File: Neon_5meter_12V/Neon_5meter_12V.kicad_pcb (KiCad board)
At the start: 2 copper layers, 46 parts, among them J1 Conn_01x16_Pin, J2 Barrel_Jack_MountingPin, J3 Conn_01x16_Pin, J4 Barrel_Jack_MountingPin, J5 Barrel_Jack_MountingPin, J6 Conn_01x03_Pin, Q1 IRLML2502TRPBF, Q2 IRLML2502TRPBF, Q3 BSS138, Q4 BSS138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

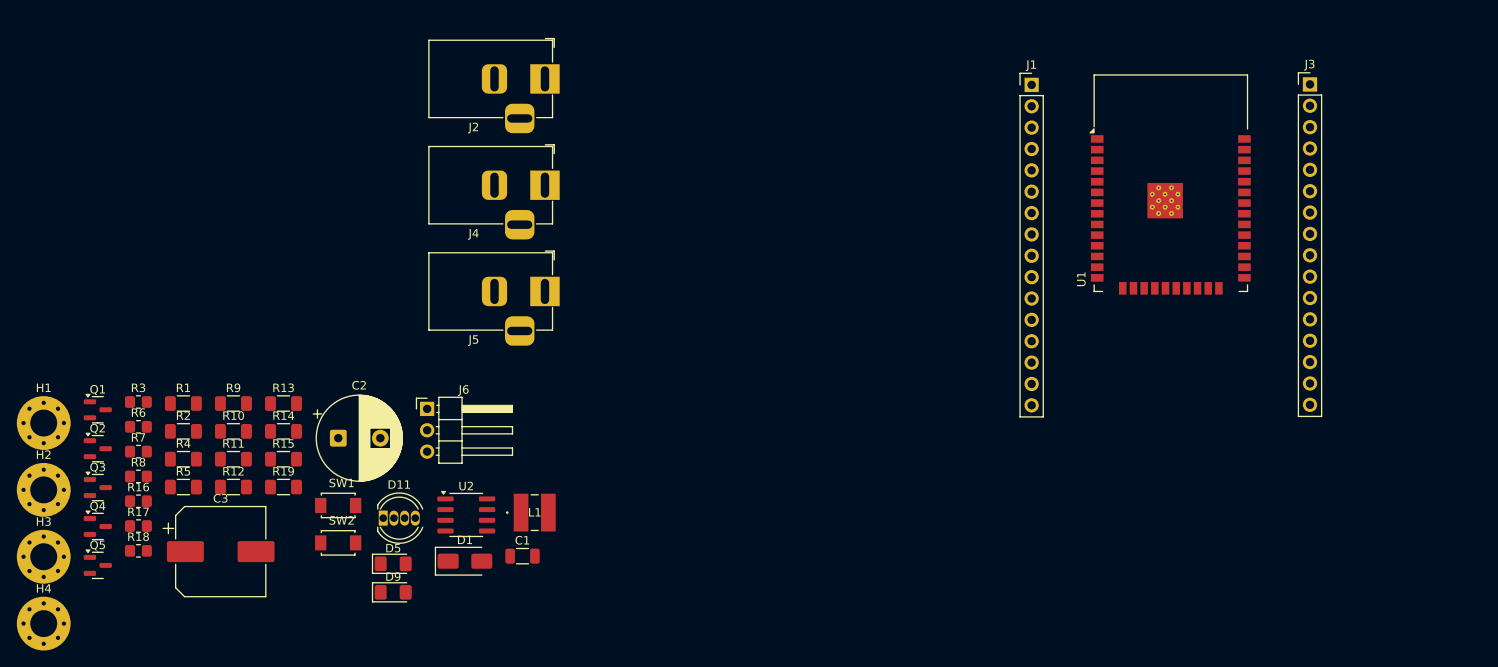
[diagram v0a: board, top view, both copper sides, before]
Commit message: updated component placement
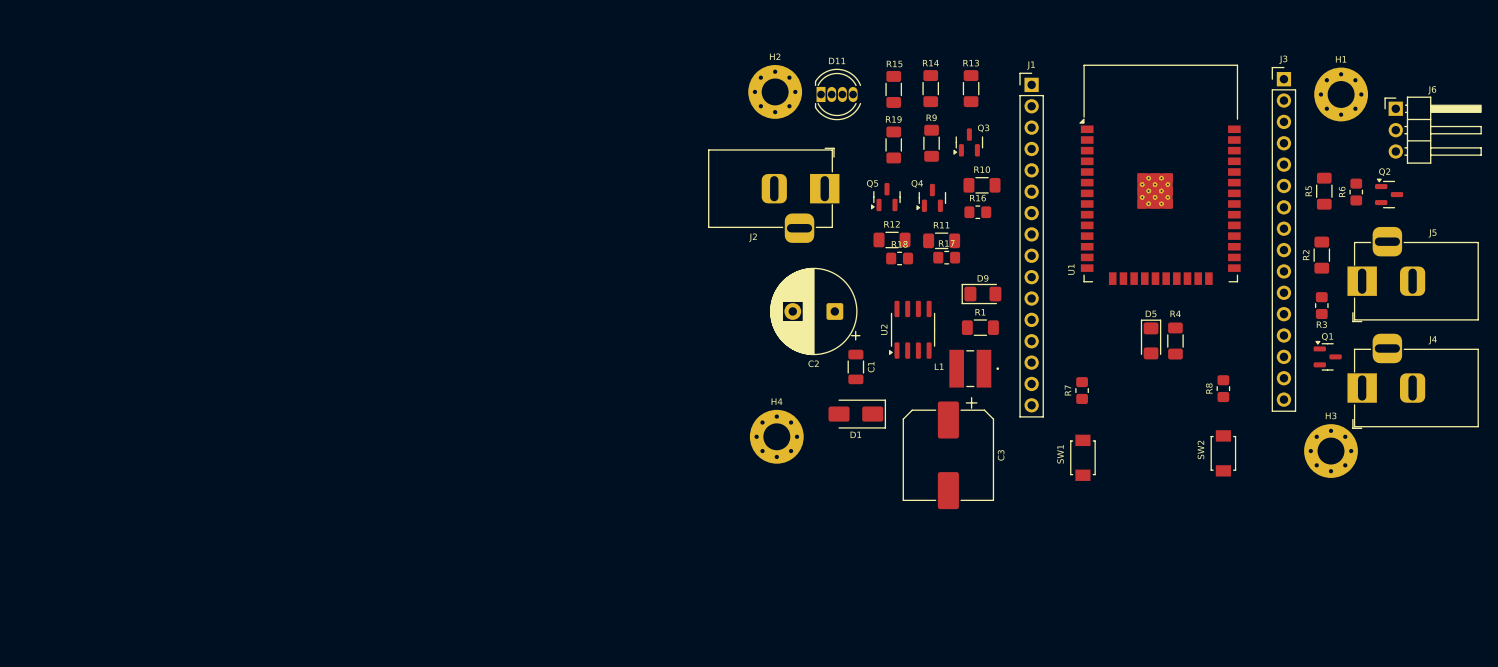
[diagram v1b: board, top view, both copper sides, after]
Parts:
- moved H1 159.1 mm to (183.6, 38.1)
- moved Q2 156.5 mm to (189.3, 50.0)
- moved H3 153.6 mm to (182.4, 80.5)
- moved R6 147.5 mm to (185.4, 49.7), turned to 90 degrees
- moved Q1 146.4 mm to (182.0, 69.3)
- moved R3 141.2 mm to (181.3, 63.2), turned to -90 degrees
- moved R5 140.1 mm to (181.6, 49.6), turned to 90 degrees
- moved R2 137.0 mm to (181.3, 57.2), turned to 90 degrees
- moved R8 129.4 mm to (169.6, 73.1), turned to 90 degrees
- moved J6 120.6 mm to (190.1, 39.8)
- moved R4 118.8 mm to (163.9, 67.4), turned to 90 degrees
- moved R7 112.4 mm to (152.8, 73.3), turned to 90 degrees
- moved Q3 111.5 mm to (139.4, 43.8), turned to 90 degrees
- moved Q4 106.6 mm to (135.0, 50.4), turned to 90 degrees
- moved SW2 105.8 mm to (169.6, 80.8), turned to 90 degrees
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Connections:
- R5 pad 2: ESP_IO18 -> ESP_IO19

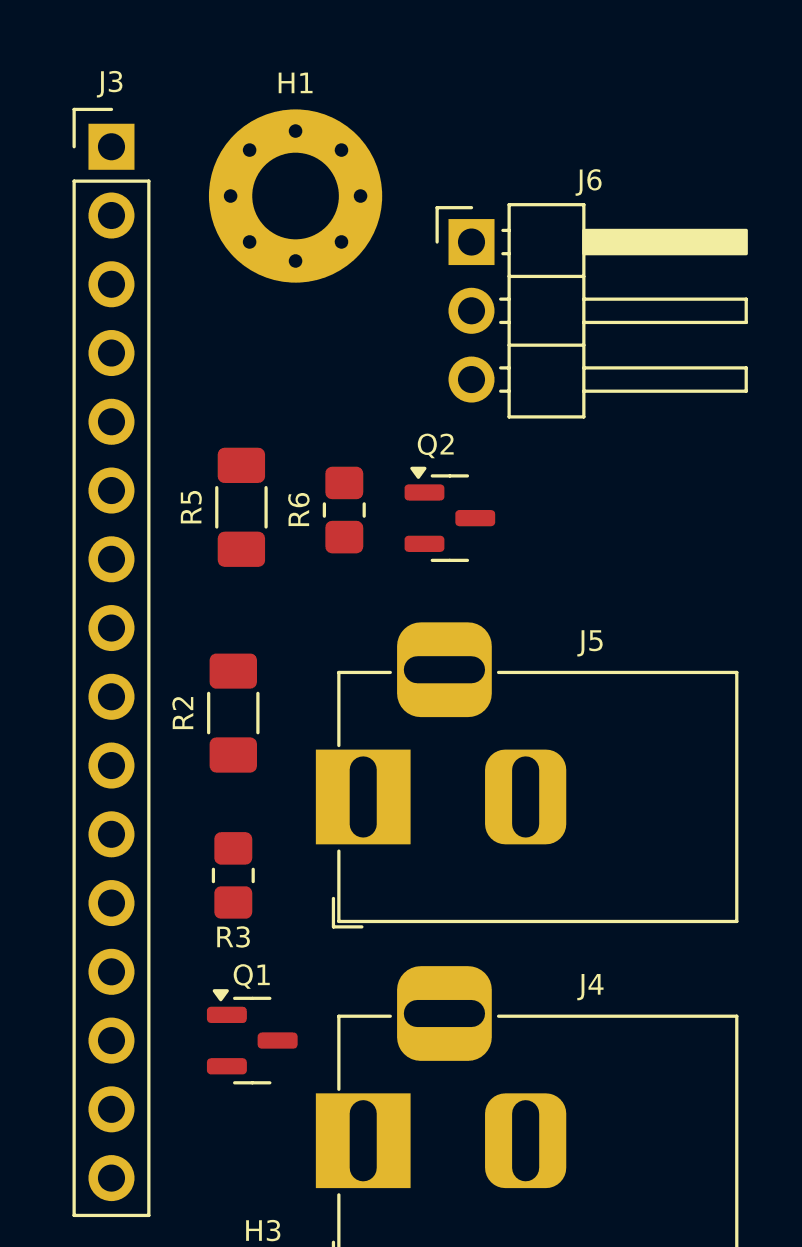
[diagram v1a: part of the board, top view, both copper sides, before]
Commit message: updated 1x3 pin header jst connector footprint
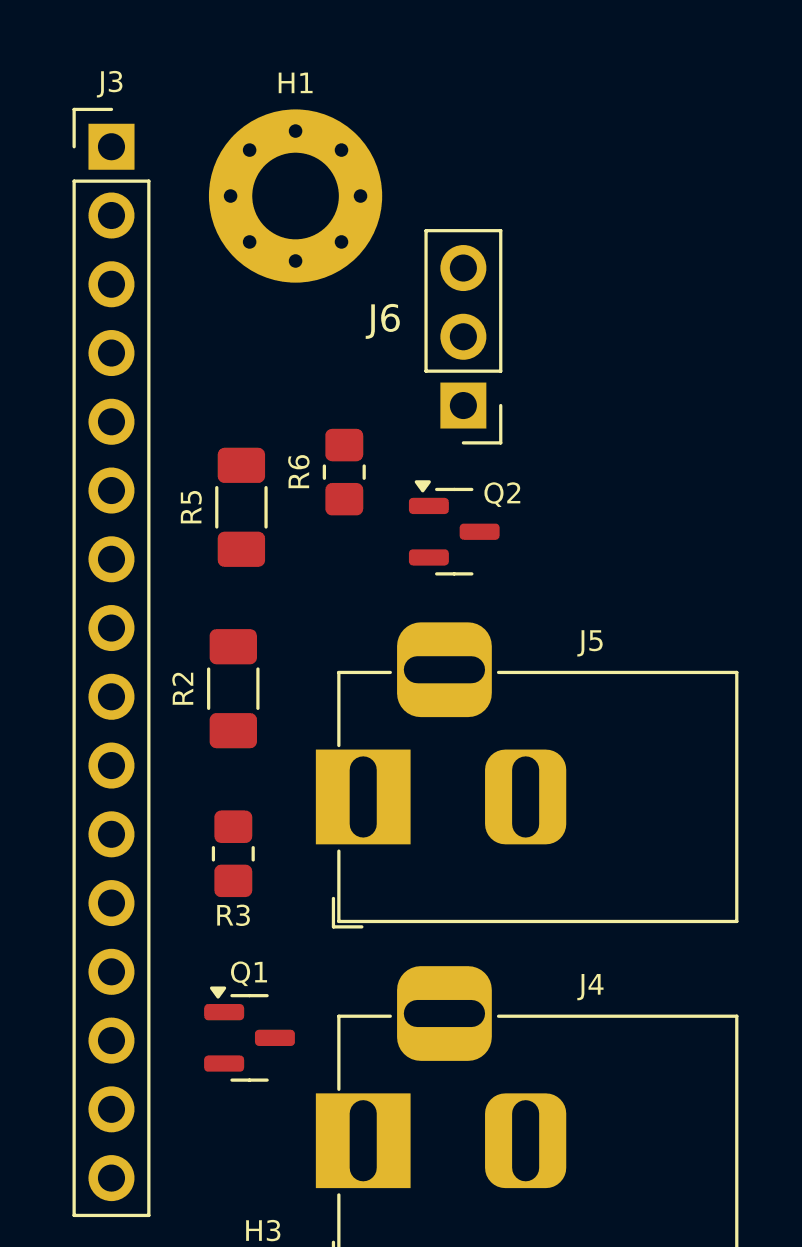
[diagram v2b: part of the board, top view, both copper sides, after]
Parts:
- J6: footprint Connector_PinHeader_2.54mm:PinHeader_1x03_P2.54mm_Horizontal -> Connector_PinHeader_2.54mm:PinHeader_1x03_P2.54mm_Vertical
- moved J6 6.05 mm to (189.8, 45.8), turned to 180 degrees
- moved R6 1.40 mm to (185.4, 48.3)
- moved R2 0.90 mm to (181.3, 56.3)
- moved R3 0.80 mm to (181.3, 62.4)
- moved Q2 0.53 mm to (189.5, 50.5)
- moved Q1 0.14 mm to (181.9, 69.2)

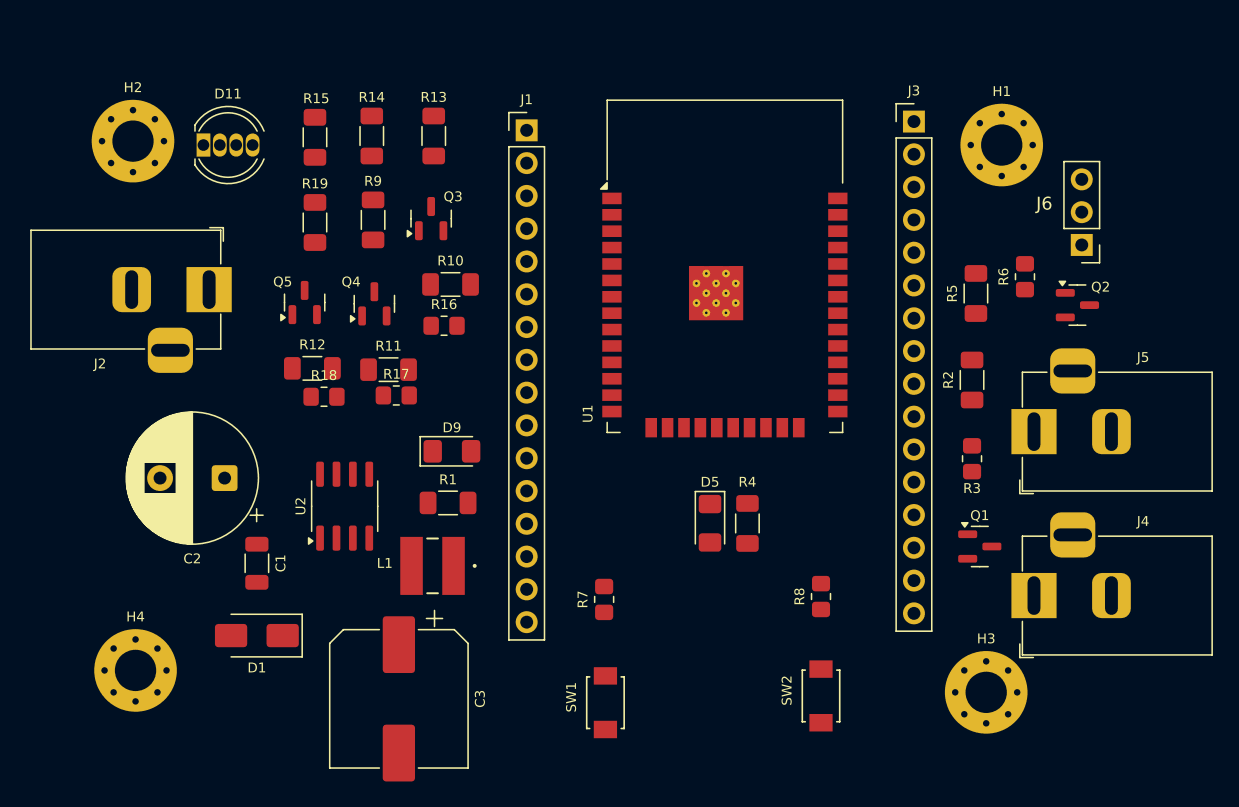
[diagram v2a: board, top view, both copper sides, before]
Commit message: updated placement removed pinheaders
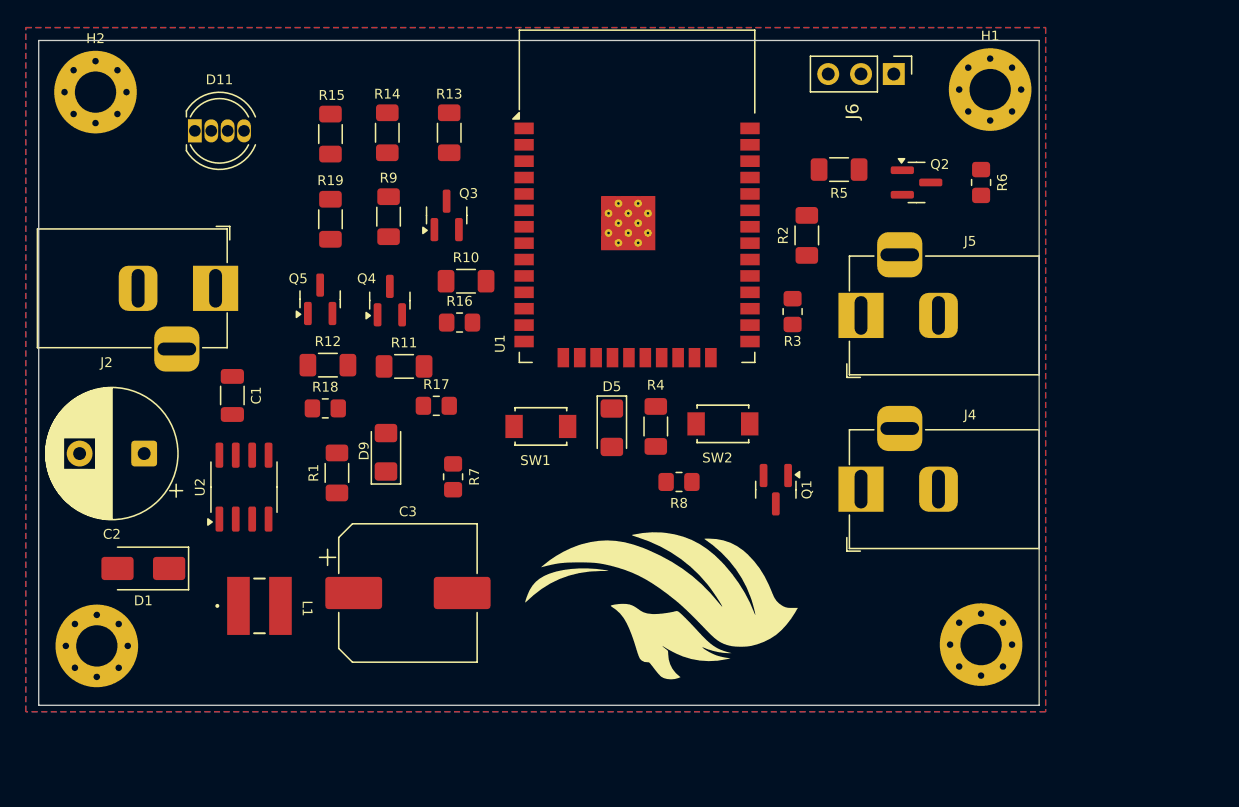
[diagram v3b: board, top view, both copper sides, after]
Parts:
- removed J1, J3: Conn_01x16_Pin, Connector_PinHeader_2.54mm:PinHeader_1x16_P2.54mm_Vertical
- added G***: LOGO, LOGO, F.Cu at (157.2, 72.9)
- moved SW2 22.4 mm to (162.0, 59.7), turned to 180 degrees
- moved SW1 22.0 mm to (147.9, 59.9), turned to 180 degrees
- moved J6 19.7 mm to (175.2, 32.6), turned to -90 degrees
- moved R3 18.0 mm to (167.4, 51.0)
- moved R2 17.0 mm to (168.5, 45.1)
- moved Q1 16.4 mm to (166.1, 64.8), turned to -90 degrees
- moved J5 16.1 mm to (172.7, 51.3)
- moved J4 15.7 mm to (172.7, 64.8)
- moved Q2 15.7 mm to (177.0, 41.0)
- moved R7 15.1 mm to (141.1, 63.8), turned to -90 degrees
- moved R5 14.3 mm to (171.0, 40.0), turned to 180 degrees
- moved R8 14.1 mm to (158.6, 64.2), turned to 180 degrees
- moved L1 13.8 mm to (126.1, 73.8), turned to 0 degrees
- moved C1 13.1 mm to (124.0, 57.5)
- moved D5 10.6 mm to (153.4, 60.0)
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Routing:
- added copper zone on B.Cu, net GND
- added copper zone on F.Cu, net GND
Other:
- board outline added: 77.5 x 51.5 mm

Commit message: updated logos and added pharohs logo
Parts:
- removed the G*** at (157.2, 72.9)
- added G***: LOGO, LOGO, F.Cu at (138.0, 56.2)
- added G***: LOGO, LOGO, F.Cu at (153.0, 72.0)
- added G***: LOGO, LOGO, F.Cu at (162.6, 74.7)
- moved C2 1.20 mm to (118.4, 62.0)
- moved U2 1.17 mm to (126.0, 65.0)
- moved R10 0.65 mm to (141.4, 48.6)
- moved R16 0.15 mm to (141.6, 52.0)
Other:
- board text added: "E Adel"
- board text added: "Made on Earth by Pharoaphs"
